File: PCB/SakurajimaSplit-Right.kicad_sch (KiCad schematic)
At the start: 43 parts, among them J15 SWD, J16 Conn_01x01_Pin, J17 Conn_01x01_Pin, J18 Conn_01x01_Pin, J20 Conn_01x01_Pin, J21 Conn_01x01_Pin, J22 Conn_01x01_Pin, J23 Conn_01x01_Pin, J24 Conn_01x01_Pin, J25 Conn_01x01_Pin, J26 Conn_01x01_Pin, J27 Conn_01x01_Pin, J28 Conn_01x01_Pin, J29 Conn_01x01_Pin, J30 Conn_01x01_Pin, SW2 SWCLK/BOOT0, U11 ZJY_M233, U6 STM32G0B1CBT6, U7 W25Q128JVS, Y2 8MHz

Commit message: fix(sch): remove encoder net labels, update mountinghole footprints
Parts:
- added J27, J28, J29: Conn_01x01_Pin, Connector_Wire:SolderWirePad_1x01_SMD_1x2mm, symbol Connector:Conn_01x01_Pin
- H5, H6, H7, H8: footprint MountingHole:MountingHole_3.2mm_M3_Pad -> MountingHole:MountingHole_3.2mm_M3_Pad_Via
- renumbered J27 to J30, J28 to J35, J29 to J36, J30 to J37
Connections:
- net Knob_A: no longer names the net of U6.1 (PC13)
- net Knob_A: now also J27.1 (Pin_1)
- net Knob_B: no longer names the net of U6.2 (PC14)
- net Knob_B: now also J28.1 (Pin_1)
- net Knob_SW: no longer names the net of U6.3 (PC15)
- net Knob_SW: now also J29.1 (Pin_1)
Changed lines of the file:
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@@
 	(wire
 		(pts
-			(xy 237.49 195.58) (xy 240.03 195.58)
+			(xy 176.53 149.86) (xy 181.61 149.86)
 		)
 		(stroke
@@
 	(wire
 		(pts
-			(xy 332.74 38.1) (xy 332.74 40.64)
+			(xy 237.49 195.58) (xy 240.03 195.58)
 		)
 		(stroke
@@
 	(wire
 		(pts
-			(xy 179.07 134.62) (xy 181.61 134.62)
+			(xy 332.74 38.1) (xy 332.74 40.64)
 		)
 		(stroke
@@
 	(wire
 		(pts
-			(xy 237.49 177.8) (xy 240.03 177.8)
+			(xy 179.07 134.62) (xy 181.61 134.62)
 		)
 		(stroke
@@
 	(wire
 		(pts
-			(xy 237.49 121.92) (xy 240.03 121.92)
+			(xy 237.49 177.8) (xy 240.03 177.8)
 		)
 		(stroke
@@
 	(wire
 		(pts
-			(xy 59.69 101.6) (xy 43.18 101.6)
+			(xy 237.49 121.92) (xy 240.03 121.92)
 		)
 		(stroke
@@
 	(wire
 		(pts
-			(xy 212.09 104.14) (xy 212.09 106.68)
+			(xy 59.69 101.6) (xy 43.18 101.6)
 		)
 		(stroke
@@
 	(wire
 		(pts
-			(xy 59.69 101.6) (xy 76.2 101.6)
+			(xy 212.09 104.14) (xy 212.09 106.68)
 		)
 		(stroke
@@
 	(wire
 		(pts
-			(xy 179.07 152.4) (xy 181.61 152.4)
+			(xy 59.69 101.6) (xy 76.2 101.6)
 		)
 		(stroke
@@
 	(wire
 		(pts
-			(xy 179.07 147.32) (xy 181.61 147.32)
-		)
-		(stroke
-			(width 0)
-			(type default)
-		)
-	)
-	(wire
-		(pts
 			(xy 43.18 234.95) (xy 59.69 234.95)
 		)
@@
 	(wire
 		(pts
-			(xy 179.07 149.86) (xy 181.61 149.86)
+			(xy 176.53 147.32) (xy 181.61 147.32)
 		)
 		(stroke
@@
 	(wire
 		(pts
+			(xy 176.53 152.4) (xy 181.61 152.4)
+		)
+		(stroke
+			(width 0)
+			(type default)
+		)
+	)
+	(wire
+		(pts
 			(xy 71.12 165.1) (xy 73.66 165.1)
 		)
@@
 		)
 	)
-	(label "Knob_SW"
-		(at 179.07 152.4 180)
-		(effects
-			(font
-				(size 1.27 1.27)
-				(thickness 0.254)
-				(bold yes)
-			)
-			(justify right bottom)
-		)
-	)
 	(label "Display_SCLK"
 		(at 43.18 232.41 180)
@@
 		)
 	)
-	(label "Knob_A"
-		(at 179.07 147.32 180)
-		(effects
-			(font
-				(size 1.27 1.27)
-				(thickness 0.254)
-				(bold yes)
-			)
-			(justify right bottom)
-		)
-	)
 	(label "ROW3"
 		(at 179.07 137.16 180)
@@
 		)
 	)
-	(label "Knob_B"
-		(at 179.07 149.86 180)
-		(effects
-			(font
-				(size 1.27 1.27)
-				(thickness 0.254)
-				(bold yes)
-			)
-			(justify right bottom)
-		)
-	)
 	(label "COL1"
 		(at 340.36 73.66 180)
@@
 	)
 	(symbol
+		(lib_id "Connector:Conn_01x01_Pin")
+		(at 171.45 152.4 0)
+		(mirror x)
+		(unit 1)
+		(exclude_from_sim no)
+		(in_bom no)
+		(on_board yes)
+		(dnp no)
+		(property "Reference" "J29"
+			(at 169.672 150.876 0)
+			(effects
+				(font
+					(size 1.27 1.27)
+				)
+			)
+		)
+		(property "Value" "Conn_01x01_Pin"
+			(at 159.004 150.876 0)
+			(effects
+				(font
+					(size 1.27 1.27)
+				)
+			)
+		)
+		(property "Footprint" "Connector_Wire:SolderWirePad_1x01_SMD_1x2mm"
+			(at 171.45 152.4 0)
+			(effects
+				(font
+					(size 1.27 1.27)
+					(thickness 0.254)
+					(bold yes)
+				)
+				(hide yes)
+			)
+		)
+		(property "Datasheet" "~"
+			(at 171.45 152.4 0)
+			(effects
+				(font
+					(size 1.27 1.27)
+					(thickness 0.254)
+					(bold yes)
+				)
+				(hide yes)
+			)
+		)
+		(property "Description" "Generic connector, single row, 01x01, script generated"
+			(at 171.45 152.4 0)
+			(effects
+				(font
+					(size 1.27 1.27)
+					(thickness 0.254)
+					(bold yes)
+				)
+				(hide yes)
+			)
+		)
+		(pin "1"
+		)
+		(instances
+			(project "SakurajimaSplit"
+				(path "/2049b6de-7453-46e1-ab60-70116abff9d6/2fb40ee0-3e4b-4e2d-8d4c-b78786a3c10e"
+					(reference "J29")
+					(unit 1)
+				)
+			)
+		)
+	)
+	(symbol
 		(lib_id "power:+3.3V")
 		(at 83.82 144.78 0)
@@
 			)
 		)
-		(property "Footprint" "MountingHole:MountingHole_3.2mm_M3_Pad"
+		(property "Footprint" "MountingHole:MountingHole_3.2mm_M3_Pad_Via"
 			(at 379.73 26.67 0)
 			(effects
@@
 	(symbol
 		(lib_id "Connector:Conn_01x01_Pin")
+		(at 171.45 149.86 0)
+		(mirror x)
+		(unit 1)
+		(exclude_from_sim no)
+		(in_bom no)
+		(on_board yes)
+		(dnp no)
+		(property "Reference" "J28"
+			(at 169.672 148.336 0)
+			(effects
+				(font
+					(size 1.27 1.27)
+				)
+			)
+		)
+		(property "Value" "Conn_01x01_Pin"
+			(at 159.004 148.336 0)
+			(effects
+				(font
+					(size 1.27 1.27)
+				)
+			)
+		)
+		(property "Footprint" "Connector_Wire:SolderWirePad_1x01_SMD_1x2mm"
+			(at 171.45 149.86 0)
+			(effects
+				(font
+					(size 1.27 1.27)
+					(thickness 0.254)
+					(bold yes)
+				)
+				(hide yes)
+			)
+		)
+		(property "Datasheet" "~"
+			(at 171.45 149.86 0)
+			(effects
+				(font
+					(size 1.27 1.27)
+					(thickness 0.254)
+					(bold yes)
+				)
+				(hide yes)
+			)
+		)
+		(property "Description" "Generic connector, single row, 01x01, script generated"
+			(at 171.45 149.86 0)
+			(effects
+				(font
+					(size 1.27 1.27)
+					(thickness 0.254)
+					(bold yes)
+				)
+				(hide yes)
+			)
+		)
+		(pin "1"
+		)
+		(instances
+			(project "SakurajimaSplit"
+				(path "/2049b6de-7453-46e1-ab60-70116abff9d6/2fb40ee0-3e4b-4e2d-8d4c-b78786a3c10e"
+					(reference "J28")
+					(unit 1)
+				)
+			)
+		)
+	)
+	(symbol
+		(lib_id "Connector:Conn_01x01_Pin")
 		(at 171.45 144.78 0)
 		(mirror x)
@@
 			)
 		)
-		(property "Footprint" "MountingHole:MountingHole_3.2mm_M3_Pad"
+		(property "Footprint" "MountingHole:MountingHole_3.2mm_M3_Pad_Via"
 			(at 379.73 41.91 0)
 			(effects
@@
 			)
 		)
-		(property "Footprint" "MountingHole:MountingHole_3.2mm_M3_Pad"
+		(property "Footprint" "MountingHole:MountingHole_3.2mm_M3_Pad_Via"
 			(at 379.73 34.29 0)
 			(effects
@@
 			)
 		)
-		(property "Footprint" "MountingHole:MountingHole_3.2mm_M3_Pad"
+		(property "Footprint" "MountingHole:MountingHole_3.2mm_M3_Pad_Via"
 			(at 379.73 49.53 0)
 			(effects
@@
 		(on_board yes)
 		(dnp no)
-		(property "Reference" "J29"
+		(property "Reference" "J36"
 			(at 249.428 163.576 0)
 			(effects
@@
 			(project "SakurajimaSplit"
 				(path "/2049b6de-7453-46e1-ab60-70116abff9d6/2fb40ee0-3e4b-4e2d-8d4c-b78786a3c10e"
-					(reference "J29")
+					(reference "J36")
 					(unit 1)
 				)
@@
 		(on_board yes)
 		(dnp no)
-		(property "Reference" "J27"
+		(property "Reference" "J30"
 			(at 249.428 150.876 0)
 			(effects
@@
 			(project "SakurajimaSplit"
 				(path "/2049b6de-7453-46e1-ab60-70116abff9d6/2fb40ee0-3e4b-4e2d-8d4c-b78786a3c10e"
+					(reference "J30")
+					(unit 1)
+				)
+			)
+		)
+	)
+	(symbol
+		(lib_id "Connector:Conn_01x01_Pin")
+		(at 171.45 147.32 0)
+		(mirror x)
+		(unit 1)
+		(exclude_from_sim no)
+		(in_bom no)
+		(on_board yes)
+		(dnp no)
+		(property "Reference" "J27"
+			(at 169.672 145.796 0)
+			(effects
+				(font
+					(size 1.27 1.27)
+				)
+			)
+		)
+		(property "Value" "Conn_01x01_Pin"
+			(at 159.004 145.796 0)
+			(effects
+				(font
+					(size 1.27 1.27)
+				)
+			)
+		)
+		(property "Footprint" "Connector_Wire:SolderWirePad_1x01_SMD_1x2mm"
+			(at 171.45 147.32 0)
+			(effects
+				(font
+					(size 1.27 1.27)
+					(thickness 0.254)
+					(bold yes)
+				)
+				(hide yes)
+			)
+		)
+		(property "Datasheet" "~"
+			(at 171.45 147.32 0)
+			(effects
+				(font
+					(size 1.27 1.27)
+					(thickness 0.254)
+					(bold yes)
+				)
+				(hide yes)
+			)
+		)
+		(property "Description" "Generic connector, single row, 01x01, script generated"
+			(at 171.45 147.32 0)
+			(effects
+				(font
+					(size 1.27 1.27)
+					(thickness 0.254)
+					(bold yes)
+				)
+				(hide yes)
+			)
+		)
+		(pin "1"
+		)
+		(instances
+			(project "SakurajimaSplit"
+				(path "/2049b6de-7453-46e1-ab60-70116abff9d6/2fb40ee0-3e4b-4e2d-8d4c-b78786a3c10e"
 					(reference "J27")
 					(unit 1)
@@
 		(on_board yes)
 		(dnp no)
-		(property "Reference" "J28"
+		(property "Reference" "J35"
 			(at 249.428 155.956 0)
 			(effects
@@
 			(project "SakurajimaSplit"
 				(path "/2049b6de-7453-46e1-ab60-70116abff9d6/2fb40ee0-3e4b-4e2d-8d4c-b78786a3c10e"
-					(reference "J28")
+					(reference "J35")
 					(unit 1)
 				)
@@
 		(on_board yes)
 		(dnp no)
-		(property "Reference" "J30"
+		(property "Reference" "J37"
 			(at 249.428 191.516 0)
 			(effects
@@
 			(project "SakurajimaSplit"
 				(path "/2049b6de-7453-46e1-ab60-70116abff9d6/2fb40ee0-3e4b-4e2d-8d4c-b78786a3c10e"
-					(reference "J30")
+					(reference "J37")
 					(unit 1)
 				)

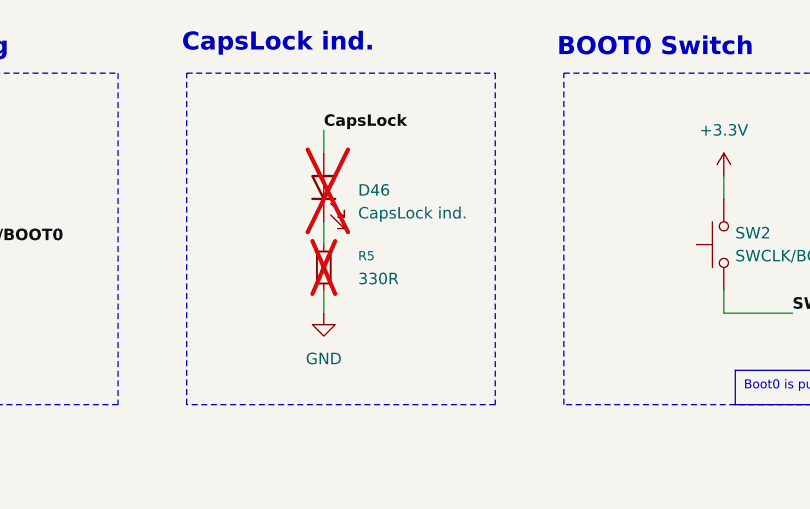
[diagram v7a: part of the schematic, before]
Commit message: fix(sch): swap LEDs with their series resistors
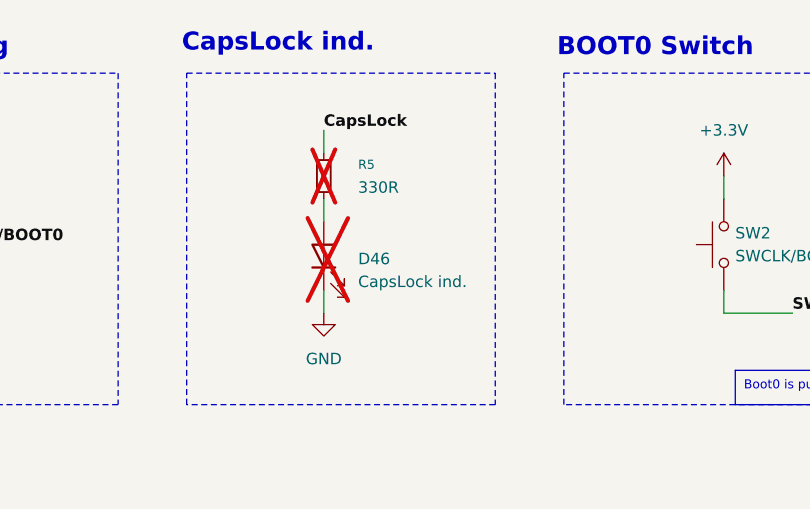
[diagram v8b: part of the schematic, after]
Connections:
- net CapsLock: now also R5.1; no longer D46.2 (A)
- net GND: now also D46.1 (K); no longer R5.2
- new net: D46.2 (A), R5.2
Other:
- moved on the sheet: D46, R5
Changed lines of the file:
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@@
 	(wire
 		(pts
-			(xy 87.63 44.45) (xy 87.63 46.99)
-		)
-		(stroke
-			(width 0)
-			(type default)
-		)
-	)
-	(wire
-		(pts
 			(xy 181.61 142.24) (xy 176.53 142.24)
 		)
@@
 	(wire
 		(pts
+			(xy 87.63 41.91) (xy 87.63 44.45)
+		)
+		(stroke
+			(width 0)
+			(type default)
+		)
+	)
+	(wire
+		(pts
 			(xy 44.45 162.56) (xy 48.26 162.56)
 		)
@@
 	(symbol
 		(lib_id "Device:R_Small")
-		(at 87.63 49.53 0)
+		(at 87.63 39.37 0)
 		(unit 1)
 		(exclude_from_sim no)
@@
 		(fields_autoplaced yes)
 		(property "Reference" "R5"
-			(at 91.44 48.2599 0)
+			(at 91.44 38.0999 0)
 			(effects
 				(font
@@
 		)
 		(property "Value" "330R"
-			(at 91.44 50.7999 0)
+			(at 91.44 40.6399 0)
 			(effects
 				(font
@@
 		)
 		(property "Footprint" "Resistor_SMD:R_0603_1608Metric"
-			(at 87.63 49.53 0)
+			(at 87.63 39.37 0)
 			(effects
 				(font
@@
 		)
 		(property "Datasheet" "~"
-			(at 87.63 49.53 0)
+			(at 87.63 39.37 0)
 			(effects
 				(font
@@
 		)
 		(property "Description" "Resistor, small symbol"
-			(at 87.63 49.53 0)
+			(at 87.63 39.37 0)
 			(effects
 				(font
@@
 		)
 		(property "Distributor Link" "https://lionelectronic.ir/products/1182-SER0603F330R"
-			(at 87.63 49.53 0)
+			(at 87.63 39.37 0)
 			(effects
 				(font
@@
 		)
 		(property "Manufacturer" "VO Sub Brand (ER)"
-			(at 87.63 49.53 0)
+			(at 87.63 39.37 0)
 			(effects
 				(font
@@
 		)
 		(property "Manufacturer Part No." "SER0603F330R"
-			(at 87.63 49.53 0)
+			(at 87.63 39.37 0)
 			(effects
 				(font
@@
 	(symbol
 		(lib_id "Device:LED")
-		(at 87.63 40.64 90)
+		(at 87.63 48.26 90)
 		(unit 1)
 		(exclude_from_sim no)
@@
 		(fields_autoplaced yes)
 		(property "Reference" "D46"
-			(at 91.44 40.9574 90)
+			(at 91.44 48.5774 90)
 			(effects
 				(font
@@
 		)
 		(property "Value" "CapsLock ind."
-			(at 91.44 43.4974 90)
+			(at 91.44 51.1174 90)
 			(effects
 				(font
@@
 		)
 		(property "Footprint" "LED_SMD:LED_0603_1608Metric"
-			(at 87.63 40.64 0)
+			(at 87.63 48.26 0)
 			(effects
 				(font
@@
 		)
 		(property "Datasheet" "~"
-			(at 87.63 40.64 0)
+			(at 87.63 48.26 0)
 			(effects
 				(font
@@
 		)
 		(property "Description" "Light emitting diode"
-			(at 87.63 40.64 0)
+			(at 87.63 48.26 0)
 			(effects
 				(font
@@
 		)
 		(property "Sim.Pins" "1=K 2=A"
-			(at 87.63 40.64 0)
+			(at 87.63 48.26 0)
 			(effects
 				(font
@@
 		)
 		(property "Distributor Link" "https://lionelectronic.ir/products/2215-XL-1608UWC-04"
-			(at 87.63 40.64 90)
+			(at 87.63 48.26 90)
 			(effects
 				(font
@@
 		)
 		(property "Manufacturer" "XINGLIGHT"
-			(at 87.63 40.64 90)
+			(at 87.63 48.26 90)
 			(effects
 				(font
@@
 		)
 		(property "Manufacturer Part No." "XL-1608UWC-04"
-			(at 87.63 40.64 90)
+			(at 87.63 48.26 90)
 			(effects
 				(font
